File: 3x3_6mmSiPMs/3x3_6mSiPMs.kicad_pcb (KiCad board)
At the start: 2 copper layers, 36 x 36 mm, 30 parts

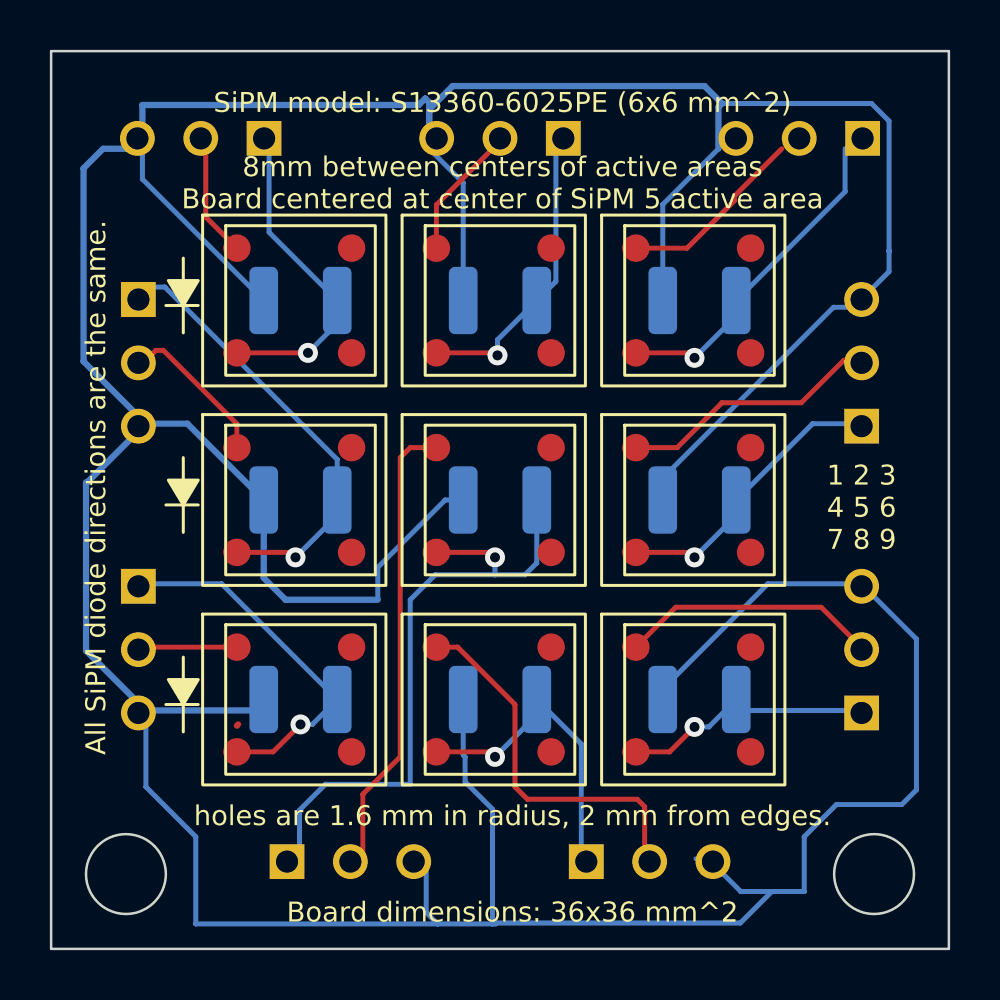
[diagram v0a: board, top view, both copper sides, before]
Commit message: new version of 3x3 6 mm SiPMs
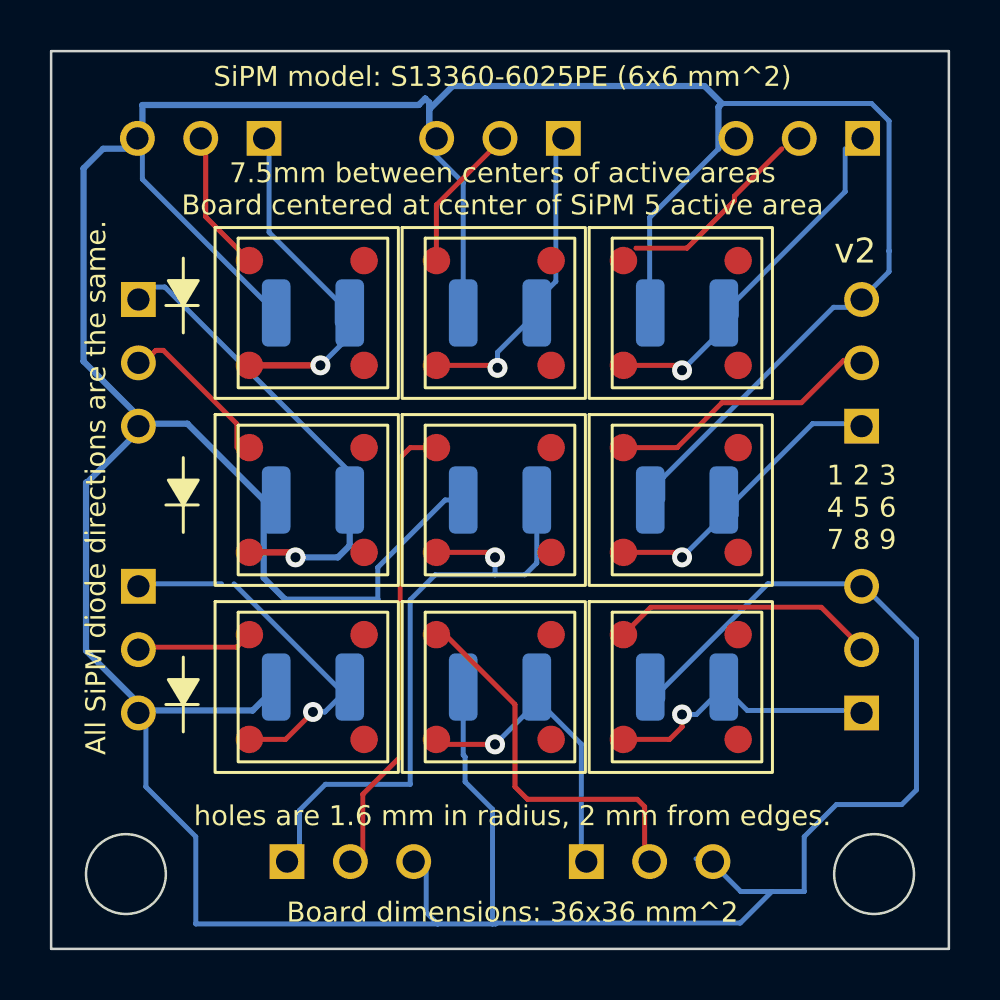
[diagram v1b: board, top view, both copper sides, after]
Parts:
- moved 10 nF 0.71 mm to (92.5, 42.5)
- moved 10 nF 0.71 mm to (107.5, 57.5)
- moved 10 nF 0.71 mm to (107.5, 42.5)
- moved 10 nF 0.71 mm to (92.5, 57.5)
- moved REF** 0.71 mm to (92.5, 42.5)
- moved REF**10 0.71 mm to (107.5, 57.5)
- moved REF**2 0.71 mm to (107.5, 42.5)
- moved REF**7 0.71 mm to (92.5, 57.5)
- moved 10 nF 0.50 mm to (100.0, 57.5)
- moved 10 nF 0.50 mm to (92.5, 50.0)
- moved 10 nF 0.50 mm to (107.5, 50.0)
- moved 10 nF 0.50 mm to (100.0, 42.5)
- moved REF**1 0.50 mm to (100.0, 42.5)
- moved REF**3 0.50 mm to (92.5, 50.0)
- moved REF**6 0.50 mm to (107.5, 50.0)
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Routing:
- net (no net): track 418.0 -> 421.9 mm
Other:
- board text added: "SiPM model: S13360-6025PE (6x6 mm^2) 7.5mm between centers of active areas Board centered at center of SiPM 5 active area"
- board text added: "v2"
- board text removed: "SiPM model: S13360-6025PE (6x6 mm^2) 8mm between centers of active areas Board centered at center of SiPM 5 active area"

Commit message: fixed broken connections on 3x3 6mm SiPM board
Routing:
- net (no net): track 421.9 -> 423.9 mm
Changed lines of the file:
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@@
+	)
+	(segment
+		(start 111.3 35.915)
+		(end 111.585 35.915)
+		(width 0.2)
+		(layer "F.Cu")
+		(net 0)
 	)
 	(segment
@@
 	)
 	(segment
+		(start 104.95 40.4)
+		(end 105.45 39.9)
+		(width 0.25)
+		(layer "F.Cu")
+		(net 0)
+	)
+	(segment
 		(start 97.45 52.1)
 		(end 99.6 52.1)
@@
 		(start 107.1 52.1)
 		(end 104.95 52.1)
+		(width 0.2)
+		(layer "F.Cu")
+		(net 0)
+	)
+	(segment
+		(start 111.585 35.915)
+		(end 112 35.5)
 		(width 0.2)
 		(layer "F.Cu")
@@
 	)
 	(segment
+		(start 89.335 53.36)
+		(end 93.975 58)
+		(width 0.2)
+		(layer "B.Cu")
+		(net 0)
+	)
+	(segment
 		(start 86.56 41.46)
 		(end 93.975 48.875)
@@
 	)
 	(segment
+		(start 85.8 53.36)
+		(end 89.335 53.36)
+		(width 0.2)
+		(layer "B.Cu")
+		(net 0)
+	)
+	(segment
 		(start 93.475 42.925)
 		(end 93.475 42)
@@
 	)
 	(segment
-		(start 89.335 53.36)
-		(end 93.975 58)
-		(width 0.2)
-		(layer "B.Cu")
-		(net 0)
-	)
-	(segment
 		(start 91.96 62.44)
 		(end 91.96 64.385)
@@
 		(width 0.2)
 		(layer "B.Cu")
-		(net 0)
-	)
-	(segment
-		(start 85.8 53.36)
-		(end 88.835 53.36)
-		(width 0.2)
-		(layer "B.Cu")

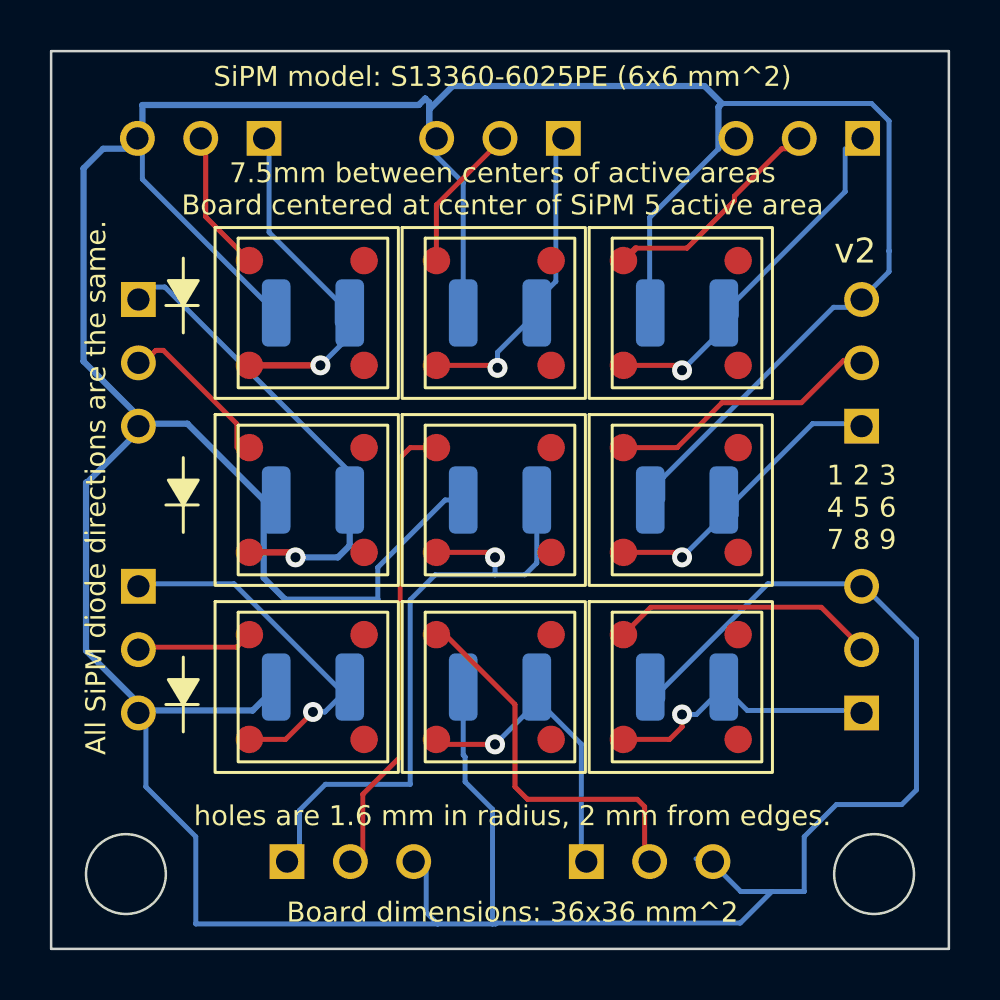
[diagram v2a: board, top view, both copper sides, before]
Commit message: fixed broken connections on 3x3 6mm SiPM board
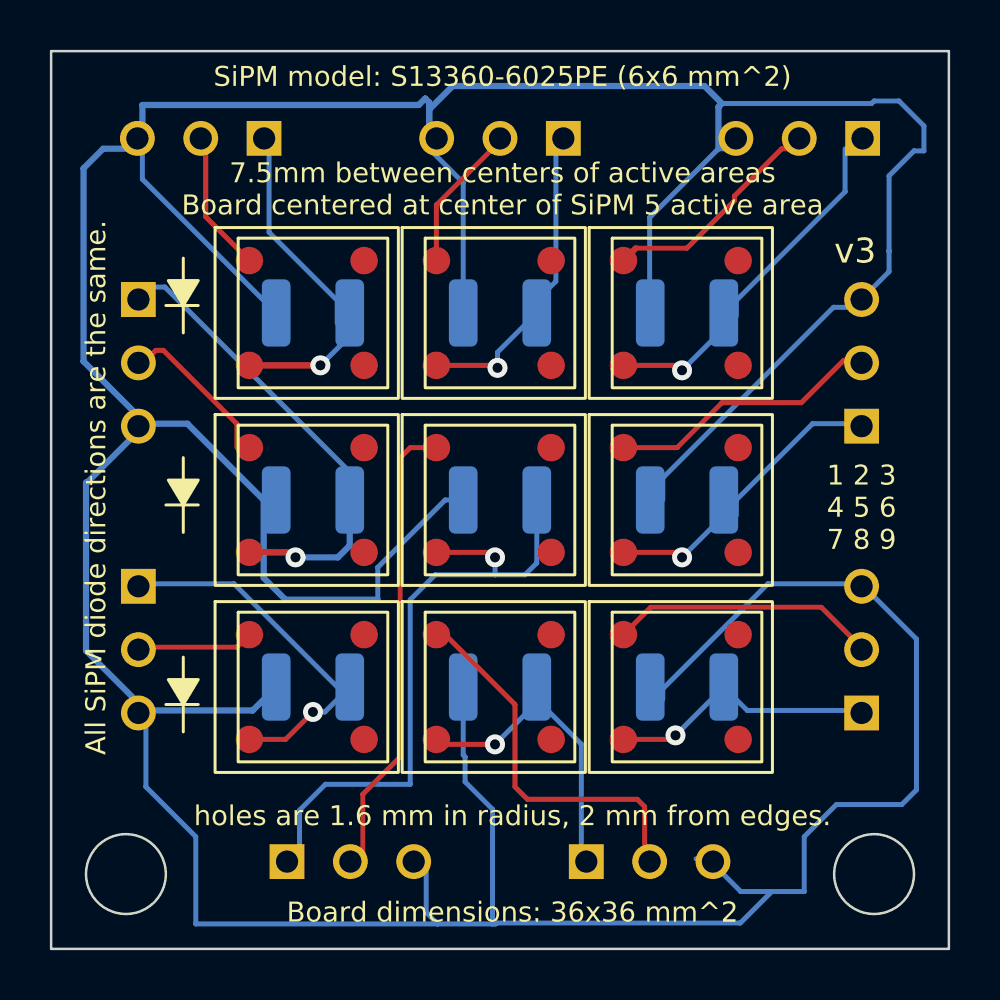
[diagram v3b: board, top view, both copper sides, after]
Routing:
- net (no net): track 423.9 -> 426.7 mm
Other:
- board text added: "All capacitors: 10 nF. v3"
- board text added: "v3"
- board text removed: "All capacitors: 10 nF"
- board text removed: "v2"
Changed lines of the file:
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@@
 		)
 	)
-	(gr_text "All capacitors: 10 nF"
+	(gr_text "All capacitors: 10 nF.  v3"
 		(at 100.2 45.5 0)
 		(layer "B.SilkS")
@@
 		)
 	)
-	(gr_text "v2"
+	(gr_text "v3"
 		(at 113.4 40.6 0)
 		(layer "F.SilkS")
@@
 	)
 	(segment
-		(start 107.3 58.6)
-		(end 107.3 59.1)
-		(width 0.2)
-		(layer "F.Cu")
-		(net 0)
-	)
-	(segment
 		(start 97.45 39.9)
 		(end 97.45 38.165)
@@
 	)
 	(segment
-		(start 107.3 59.1)
-		(end 106.8 59.6)
-		(width 0.2)
-		(layer "F.Cu")
-		(net 0)
-	)
-	(segment
 		(start 88.2 38.65)
 		(end 89.95 40.4)
@@
 	)
 	(segment
+		(start 107.0375 59.4375)
+		(end 106.875 59.6)
+		(width 0.2)
+		(layer "F.Cu")
+		(net 0)
+	)
+	(segment
 		(start 99.8 44.6)
 		(end 99.9 44.7)
@@
 	)
 	(segment
-		(start 106.8 59.6)
-		(end 104.95 59.6)
-		(width 0.2)
-		(layer "F.Cu")
-		(net 0)
-	)
-	(segment
 		(start 96 60.3)
 		(end 96 48.3)
@@
 		(start 105.5 62)
 		(end 101.1 62)
+		(width 0.2)
+		(layer "F.Cu")
+		(net 0)
+	)
+	(segment
+		(start 106.875 59.6)
+		(end 104.95 59.6)
 		(width 0.2)
 		(layer "F.Cu")
@@
 	)
 	(via
-		(at 107.3 58.6)
+		(at 107.0375 59.4375)
 		(size 0.8)
 		(drill 0.4)
@@
 	)
 	(segment
+		(start 116.6 36)
+		(end 115.6 37)
+		(width 0.2)
+		(layer "B.Cu")
+		(net 0)
+	)
+	(segment
 		(start 89.335 53.36)
 		(end 93.975 58)
@@
 	)
 	(segment
+		(start 106 38.675)
+		(end 108.675 36)
+		(width 0.2)
+		(layer "B.Cu")
+		(net 0)
+	)
+	(segment
 		(start 113.84 37.635)
 		(end 113.84 35.915)
@@
 	)
 	(segment
+		(start 116 34)
+		(end 117 35)
+		(width 0.2)
+		(layer "B.Cu")
+		(net 0)
+	)
+	(segment
 		(start 109.475 50.625)
 		(end 109.475 50)
@@
 	)
 	(segment
+		(start 108.675 36)
+		(end 108.76 35.915)
+		(width 0.2)
+		(layer "B.Cu")
+		(net 0)
+	)
+	(segment
 		(start 90.74 35.915)
 		(end 90.74 39.265)
@@
 	)
 	(segment
-		(start 115.6 34.8)
-		(end 114.9 34.1)
-		(width 0.2)
-		(layer "B.Cu")
-		(net 0)
-	)
-	(segment
 		(start 112.2 63.5)
 		(end 113.4875 62.2125)
@@
 	)
 	(segment
+		(start 108.76 35.915)
+		(end 109.045 35.915)
+		(width 0.2)
+		(layer "B.Cu")
+		(net 0)
+	)
+	(segment
 		(start 85.8 58.44)
 		(end 85.8 61.5)
@@
 	)
 	(segment
+		(start 115 34)
+		(end 116 34)
+		(width 0.2)
+		(layer "B.Cu")
+		(net 0)
+	)
+	(segment
 		(start 87.465 46.94)
 		(end 90.525 50)
@@
 	)
 	(segment
-		(start 106 38.675)
-		(end 108.76 35.915)
-		(width 0.2)
-		(layer "B.Cu")
-		(net 0)
-	)
-	(segment
 		(start 101 53)
 		(end 101.475 52.525)
@@
 	)
 	(segment
+		(start 117 35)
+		(end 117 36)
+		(width 0.2)
+		(layer "B.Cu")
+		(net 0)
+	)
+	(segment
 		(start 109.475 42.625)
 		(end 109.475 42)
@@
 	)
 	(segment
+		(start 117 36)
+		(end 116.6 36)
+		(width 0.2)
+		(layer "B.Cu")
+		(net 0)
+	)
+	(segment
 		(start 99.8625 66.9625)
 		(end 109.6375 66.9625)
@@
 	)
 	(segment
-		(start 107.875 58.6)
-		(end 108.975 57.5)
-		(width 0.2)
-		(layer "B.Cu")
-		(net 0)
-	)
-	(segment
 		(start 106.525 57.575)
 		(end 106.525 58)
@@
 	)
 	(segment
-		(start 107.3 58.6)
-		(end 107.875 58.6)
-		(width 0.2)
-		(layer "B.Cu")
-		(net 0)
-	)
-	(segment
 		(start 109.475 50)
 		(end 112.535 46.94)
@@
 	)
 	(segment
+		(start 114.9 34.1)
+		(end 115 34)
+		(width 0.2)
+		(layer "B.Cu")
+		(net 0)
+	)
+	(segment
 		(start 96.4 61.4)
 		(end 93 61.4)
@@
 	)
 	(segment
+		(start 107.0375 59.4375)
+		(end 108.975 57.5)
+		(width 0.2)
+		(layer "B.Cu")
+		(net 0)
+	)
+	(segment
 		(start 90.525 53.125)
 		(end 91.4 54)
@@
 	)
 	(segment
+		(start 115.6 40)
+		(end 115.6 37)
+		(width 0.2)
+		(layer "B.Cu")
+		(net 0)
+	)
+	(segment
 		(start 103.26 59.785)
 		(end 103.26 64.385)
@@
 	)
 	(segment
-		(start 115.6 40)
-		(end 115.6 34.8)
-		(width 0.2)
-		(layer "B.Cu")
-		(net 0)
-	)
-	(segment
 		(start 91.8 52.3)
 		(end 93.5 52.3)
@@
 		(width 0.2)
 		(layer "B.Cu")
+		(net 0)
+	)
+	(segment
+		(start 109.045 35.915)
+		(end 109.46 35.5)
+		(width 0.2)
+		(layer "B.Cu")
